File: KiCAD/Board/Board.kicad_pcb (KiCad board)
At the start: 2 copper layers, 141.2 x 154.3 mm, 104 parts, among them J1 MOTOR_5PIN_CONNECTOR, J3 BATTERY_2PIN_CONNECTOR, Q1 AO3400A, Q5 SFH309, Q7 AO3400A, Q8 SFH309, U1 4040, U10 ULN2003A, U11 CD4060BE, U2 4015, U3 LM393, U5 4040, U8 LM7805_TO220, U9 LM393, Y1 Crystal

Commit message: June 1st Updated
Greatly simplified design using ULN2003 completely and all of its pins. down to only 6 chips and 1 mosfet !!! . This will be  the last design modification. its perfect at this point
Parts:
- removed C13: C0.1uf, Capacitor_THT:C_Disc_D5.0mm_W2.5mm_P2.50mm
- removed C14: C10uf, Capacitor_THT:C_Radial_D6.3mm_H5.0mm_P2.50mm
- removed JP10, JP7, JP8, JP9: JMP, Library:Jumper
- removed Q8: SFH309, LED_THT:LED_D3.0mm_Clear
- removed R17, R19, R26, R27, R28, R30, R34, R35: R4.7K, Resistor_THT:R_Axial_DIN0207_L6.3mm_D2.5mm_P10.16mm_Horizontal
- removed U3: LM393, Package_DIP:DIP-8_W7.62mm_Socket
- added D11: D4148, Diode_THT:D_DO-35_SOD27_P12.70mm_Horizontal, F.Cu at (53.6, 133.8)
- added D12: D4148, Diode_THT:D_DO-35_SOD27_P12.70mm_Horizontal, F.Cu at (53.6, 137.3)
- added R2: R4.7K, Resistor_THT:R_Axial_DIN0207_L6.3mm_D2.5mm_P10.16mm_Horizontal, F.Cu at (53.6, 141.1)
- added R20: R47K, Resistor_THT:R_Axial_DIN0207_L6.3mm_D2.5mm_P10.16mm_Horizontal, F.Cu at (53.6, 145.2)
- added R22: R4.7K, Resistor_THT:R_Axial_DIN0207_L6.3mm_D2.5mm_P10.16mm_Horizontal, F.Cu at (53.6, 149.2)
- added R23: R4.7K, Resistor_THT:R_Axial_DIN0207_L6.3mm_D2.5mm_P10.16mm_Horizontal, F.Cu at (53.6, 153.3)
- Q1: value AO3400A -> SFH309; footprint Package_TO_SOT_SMD:SOT-23 -> LED_THT:LED_D3.0mm_Clear
- R13: value R47K -> R4.7K
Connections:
- D17 pad 1: Net-(D17-K) -> /F3
- D32 pad 1: Net-(D32-K) -> Net-(D15-K)
- D33 pad 1: Net-(D33-K) -> /F2
- Q1 pad 1: Net-(Q1-G) -> Net-(Q1-C)
- Q7 pad 3: Net-(Q5-C) -> Net-(Q1-C)
- R1 pad 1: Net-(D15-K) -> /LOAD
- R1 pad 2: Net-(Q1-G) -> +5V
- R13 pad 1: GND -> /R_RESET
- R13 pad 2: Net-(Q1-G) -> +5V
- R14 pad 1: Net-(Q1-D) -> /"R" CLOCK
- R14 pad 2: +5V -> Net-(D11-A)
- U10 pad 1: Net-(JP7-B) -> /F1
- U10 pad 10: unconnected-(U10-O7-Pad10) -> /F_RESET
- U10 pad 11: unconnected-(U10-O6-Pad11) -> /R_RESET
- U10 pad 12: unconnected-(U10-O5-Pad12) -> /LOAD
- U10 pad 5: unconnected-(U10-I5-Pad5) -> Net-(D15-K)
- U10 pad 6: unconnected-(U10-I6-Pad6) -> Net-(Q5-C)
- U10 pad 7: unconnected-(U10-I7-Pad7) -> Net-(Q1-C)
- U2 pad 15: Net-(Q1-D) -> /LOAD
- U2 pad 6: /F_RESET -> Net-(D11-K)
- U2 pad 7: Net-(Q1-D) -> /LOAD
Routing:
- net GND: track 265.9 -> 201.9 mm
- net +5V: track 168.2 -> 117.9 mm
- net Net-(JP1-B): track 38.5 -> 0.00 mm
- net Net-(Q5-C): track 26.4 -> 0.00 mm
- net Net-(U3B-+): track 7.75 -> 0.00 mm
- net Net-(Q8-C): track 4.17 -> 0.00 mm
- net Net-(D32-K): track 3.86 -> 0.00 mm
- net Net-(D15-K): track 11.7 -> 15.6 mm
- net /F_RESET: track 3.82 -> 0.00 mm
- net /R_RESET: track 3.56 -> 0.00 mm
- net /F1: track 17.0 -> 20.5 mm
- net Net-(JP7-B): track 3.55 -> 0.00 mm
- net Net-(D33-K): track 3.18 -> 0.00 mm
- net /F2: track 7.63 -> 10.8 mm
- net Net-(D17-K): track 3.05 -> 0.00 mm
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
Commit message: June 1st Project COMPLETED
Project Completed and Ready for Soldering
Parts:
- removed JP12: JMP, Library:Jumper
- added J2: MOTOR_5PIN_CONNECTOR_2, Connector_PinSocket_2.54mm:PinSocket_1x05_P2.54mm_Vertical, F.Cu at (92.2, 93.0)
- added JP10: JMP, Library:Jumper, F.Cu at (100.9, 96.7)
- added JP13: JMP, Library:Jumper, F.Cu at (59.2, 99.6)
- added JP14: JMP, Library:Jumper, F.Cu at (88.5, 96.5)
- added JP15: JMP, Library:Jumper, F.Cu at (27.8, 70.6)
- added JP16: JMP, Library:Jumper, F.Cu at (18.3, 84.3)
- added JP17: JMP, Library:Jumper, F.Cu at (16.6, 85.7)
- added JP19: JMP, Library:Jumper, F.Cu at (78.2, 23.8)
- added JP21: JMP, Library:Jumper, F.Cu at (93.1, 63.6)
- added JP7: JMP, Library:Jumper, F.Cu at (60.0, 124.0)
- added JP8: JMP, Library:Jumper, F.Cu at (18.1, 95.5)
- added JP9: JMP, Library:Jumper, F.Cu at (100.9, 94.1)
- added R17: R4.7K, Resistor_THT:R_Axial_DIN0207_L6.3mm_D2.5mm_P10.16mm_Horizontal, F.Cu at (129.2, 44.5)
- moved D1 154.0 mm to (122.4, 35.2), turned to -90 degrees
- moved D13 139.7 mm to (115.4, 35.2), turned to -90 degrees
- moved C4 106.9 mm to (119.2, 87.4), turned to 180 degrees
- moved C3 105.3 mm to (119.2, 92.8), turned to 180 degrees
- moved J3 105.2 mm to (116.7, 83.0), turned to 90 degrees
- moved U8 101.0 mm to (114.8, 99.6), turned to 180 degrees
- moved R2 98.3 mm to (108.1, 59.3), turned to -90 degrees
- moved JP6 91.6 mm to (138.3, 37.1), turned to 0 degrees
- moved C6 81.0 mm to (109.6, 88.6), turned to 0 degrees
- moved R22 75.4 mm to (103.8, 93.0), turned to 90 degrees
- moved C5 72.7 mm to (109.6, 82.7), turned to 0 degrees
- moved JP20 63.5 mm to (106.7, 30.3), turned to 0 degrees
- moved R20 56.7 mm to (39.1, 90.4), turned to 180 degrees
- moved R14 54.4 mm to (104.3, 59.3), turned to -90 degrees
- moved R23 50.9 mm to (74.9, 107.1)
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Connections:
- C1 pad 1: +5V -> /CLK_VCC
- C10 pad 1: +5V -> /CLK_VCC
- C2 pad 1: +5V -> /CLK_VCC
- C26 pad 1: Net-(JP6-A) -> +5V
- C27 pad 1: Net-(JP6-A) -> +5V
- C7 pad 1: Net-(JP6-A) -> +5V
- C8 pad 1: Net-(JP6-A) -> +5V
- C9 pad 1: +5V -> /CLK_VCC
- D1 pad 2: +5V -> /CLK_VCC
- D12 pad 2: /F_RESET -> Net-(D12-A)
- D13 pad 2: +5V -> /CLK_VCC
- D17 pad 1: /F3 -> Net-(D17-K)
- D2 pad 2: +5V -> Net-(D2-A)
- D32 pad 1: Net-(D15-K) -> Net-(D32-K)
- D33 pad 1: /F2 -> Net-(D33-K)
- J1 pad 1: Net-(J1-Pin_1) -> +5V
- JP20 pad 1: Net-(J1-Pin_1) -> +5V
- JP20 pad 2: +5V -> /CLK_VCC
- JP6 pad 1: Net-(JP6-A) -> +5V
- JP6 pad 2: +5V -> Net-(JP6-B)
- Q5 pad 1: Net-(Q5-C) -> Net-(JP7-B)
- R1 pad 1: /LOAD -> Net-(JP9-A)
- R13 pad 1: /R_RESET -> Net-(JP10-B)
- R14 pad 1: /"R" CLOCK -> Net-(U5-Q5)
- R14 pad 2: Net-(D11-A) -> /"R" CLOCK A
- R2 pad 1: Net-(Q5-C) -> Net-(U5-Q5)
- R2 pad 2: /"R" CLOCK -> /"R" CLOCK B
- R4 pad 1: Net-(JP6-A) -> +5V
- R8 pad 2: Net-(JP6-A) -> +5V
- R9 pad 2: +5V -> Net-(D2-A)
- U1 pad 16: Net-(JP6-A) -> +5V
- U10 pad 1: /F1 -> Net-(JP15-A)
- U10 pad 11: /R_RESET -> Net-(JP10-B)
- U10 pad 12: /LOAD -> Net-(JP9-A)
- U10 pad 5: Net-(D15-K) -> Net-(D32-K)
- U10 pad 6: Net-(Q5-C) -> Net-(JP7-B)
- U11 pad 16: Net-(JP6-A) -> +5V
- U2 pad 1: Net-(JP12-A) -> /MOTOR_CLOCK_B
- U5 pad 16: +5V -> /CLK_VCC
- U5 pad 2: /"R" CLOCK -> Net-(U5-Q5)
- U9 pad 4: GND -> Net-(JP21-A)
- U9 pad 8: +5V -> /CLK_VCC
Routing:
- net GND: track 201.9 -> 560.5 mm
- net Net-(JP6-A): track 73.8 -> 0.00 mm
- net +5V: track 117.9 -> 190.9 mm
- net /CLK_VCC: track 0.00 -> 47.3 mm
- net /F_RESET: track 0.00 -> 28.0 mm
- net Net-(Q1-D): track 27.6 -> 0.00 mm
- net Net-(JP1-B): track 0.00 -> 23.9 mm
- net /LOAD: track 0.00 -> 21.8 mm
- net Net-(JP10-B): track 0.00 -> 21.3 mm
- net Net-(Q1-C): track 0.00 -> 19.5 mm
- net /MOTOR_CLOCK_B: track 3.98 -> 22.1 mm
- net Net-(JP9-A): track 0.00 -> 15.4 mm
- net Net-(D11-K): track 0.00 -> 12.3 mm
- net Net-(D15-K): track 15.6 -> 3.38 mm
- net Net-(D31-A): track 12.7 -> 22.0 mm
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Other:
- board size 141.2 x 154.3 mm -> 122 x 87.5 mm
- board text added: "0BIT"
- board text added: "1BIT"
- board text added: "1MEG"
- board text added: "22pF x 2"
- board text added: "4040_11"
- board text added: "47K"
- board text added: "5V"
- board text added: "COMP7"
- board text added: "GND"
- board text added: "IR_DIODE"
- board text added: "IR_TRANSISTOR"
- board text added: "MCLKA"
- board text added: "RCLKA"
- board text added: "RCLKB"
- board text added: "ULN1"
- board text added: "ULN10"
- board text added: "ULN11"
- board text added: "ULN12"
- board text added: "ULN2"
- board text added: "ULN3"
- board text added: "ULN5"

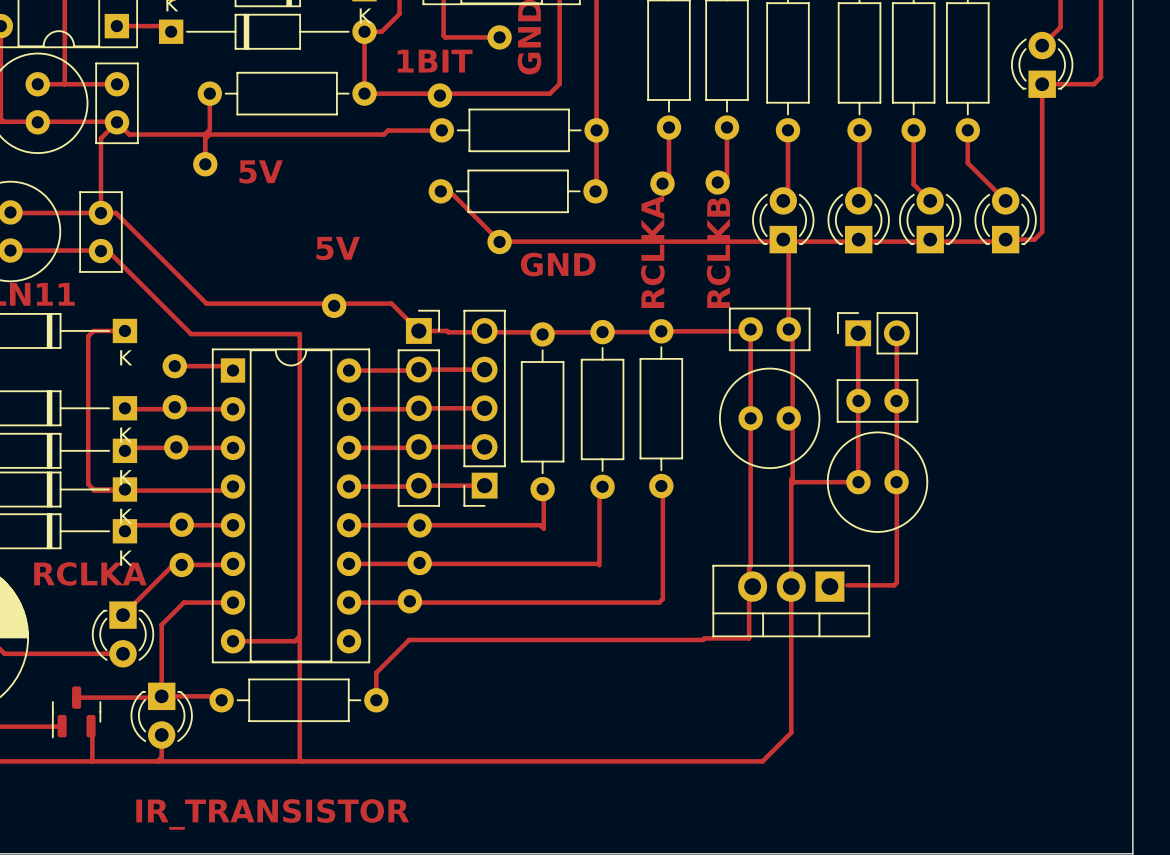
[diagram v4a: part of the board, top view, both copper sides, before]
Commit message: June 3rd 2025 Update
Added ULN2003 Pull down Resistors for Stepper Motor Control
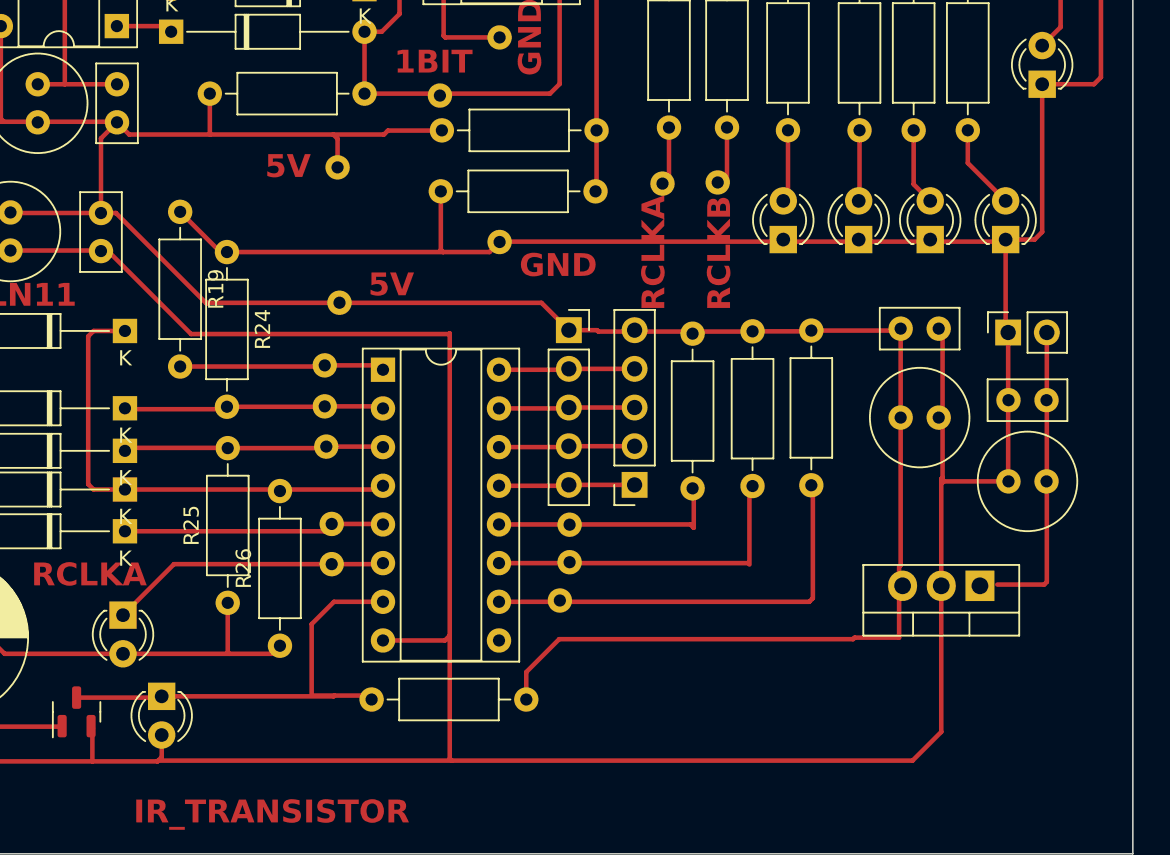
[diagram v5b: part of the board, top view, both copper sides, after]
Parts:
- added R19: R47K, Resistor_THT:R_Axial_DIN0207_L6.3mm_D2.5mm_P10.16mm_Horizontal, F.Cu at (72.2, 75.0)
- added R24: R47K, Resistor_THT:R_Axial_DIN0207_L6.3mm_D2.5mm_P10.16mm_Horizontal, F.Cu at (75.2, 77.6)
- added R25: R47K, Resistor_THT:R_Axial_DIN0207_L6.3mm_D2.5mm_P10.16mm_Horizontal, F.Cu at (75.3, 100.7)
- added R26: R47K, Resistor_THT:R_Axial_DIN0207_L6.3mm_D2.5mm_P10.16mm_Horizontal, F.Cu at (78.7, 103.5)
- moved C3 9.85 mm to (129.1, 92.7)
- moved C4 9.85 mm to (129.1, 87.4)
- moved C5 9.85 mm to (119.5, 82.7)
- moved C6 9.85 mm to (119.5, 88.5)
- moved J1 9.85 mm to (97.7, 82.8)
- moved J2 9.85 mm to (102.0, 92.9)
- moved J3 9.85 mm to (126.5, 82.9)
- moved R1 9.85 mm to (105.8, 93.2)
- moved R13 9.85 mm to (109.8, 93.0)
- moved R22 9.85 mm to (113.6, 93.0)
- moved R23 9.85 mm to (84.7, 107.0)
- moved U10 9.85 mm to (85.5, 85.4)
- moved U8 9.85 mm to (124.7, 99.6)
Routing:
- net GND: track 560.5 -> 616.5 mm
- net Net-(Q1-C): track 19.5 -> 30.9 mm
- net Net-(D32-K): track 7.26 -> 17.7 mm
- net /F2: track 7.62 -> 17.9 mm
- net /F3: track 7.37 -> 17.6 mm
- net +5V: track 190.9 -> 200.9 mm
- net Net-(JP7-B): track 8.62 -> 18.5 mm
- net Net-(JP15-A): track 3.93 -> 13.5 mm
- net /F4: track 24.0 -> 32.4 mm

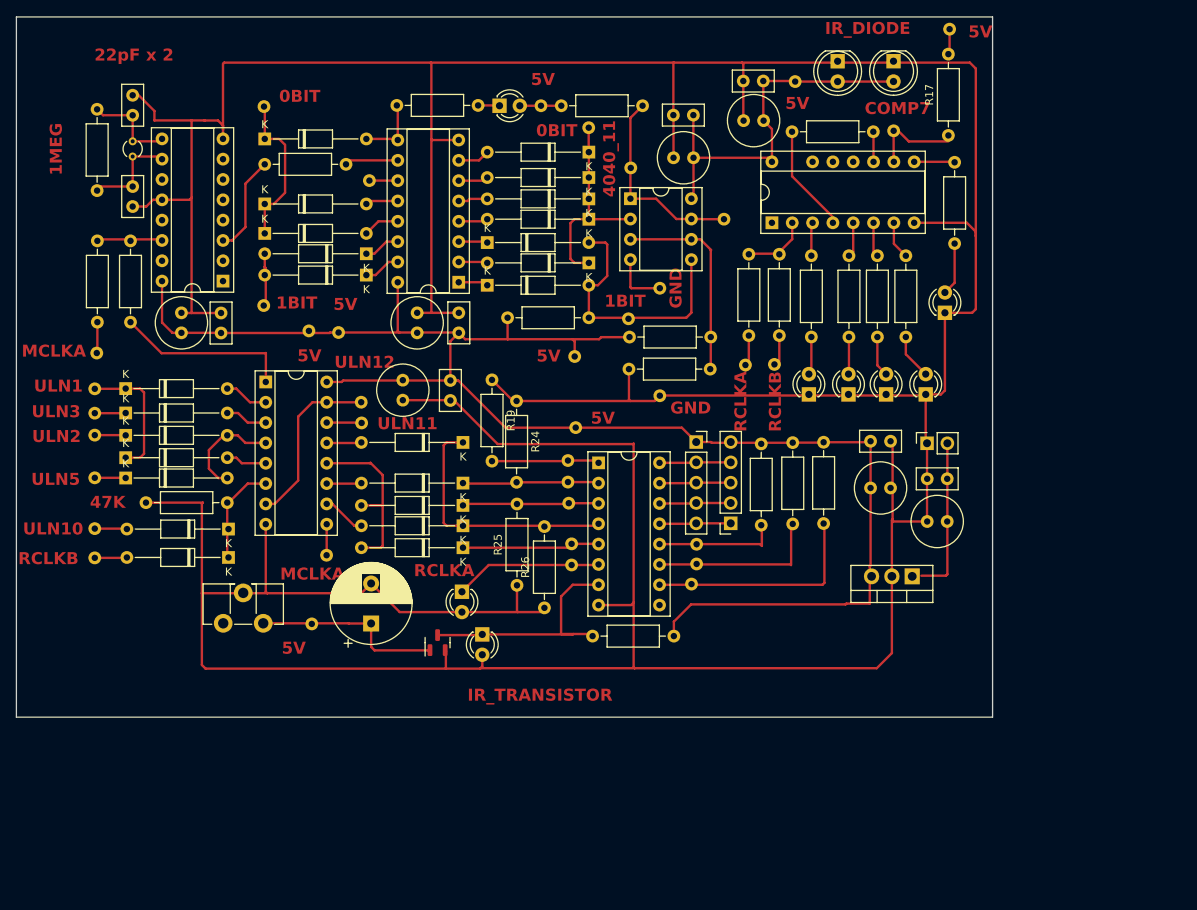
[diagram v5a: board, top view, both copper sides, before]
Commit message: 10th June 2025 Updated
Added Pull Downs 47K to ULN2003. Inverted Logic for Photo Transistors where cutting off IR rays off of photo transistors turns off forward and reverse motion since blocking IR rays is easier then reflecting it
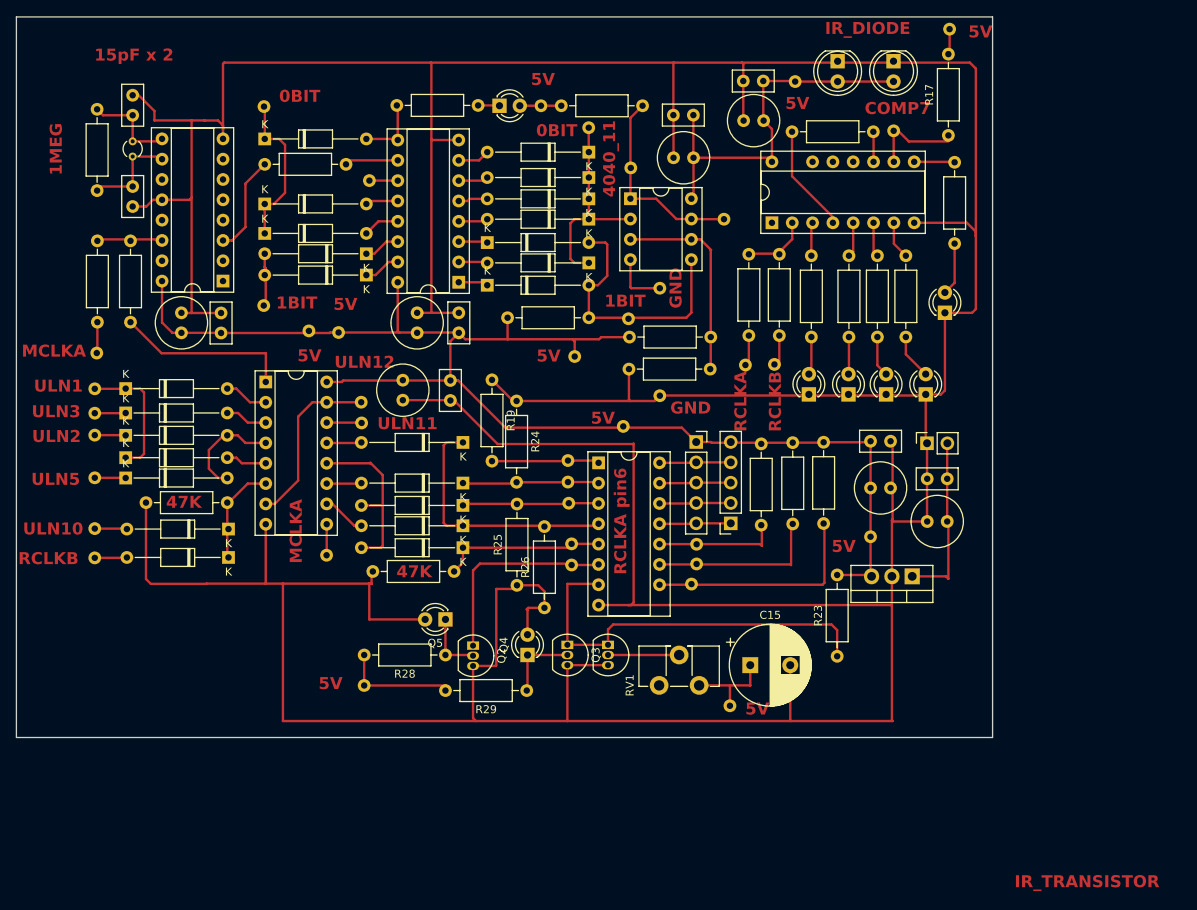
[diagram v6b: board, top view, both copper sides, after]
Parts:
- removed Q7: AO3400A, Package_TO_SOT_SMD:SOT-23
- added JP12: JMP, Library:Jumper, F.Cu at (84.1, 136.1)
- added Q2: BC547, Package_TO_SOT_THT:TO-92_Inline, F.Cu at (69.8, 108.2)
- added Q3: BC547, Package_TO_SOT_THT:TO-92_Inline, F.Cu at (81.6, 108.1)
- added Q4: SFH309, LED_THT:LED_D3.0mm_Clear, F.Cu at (76.6, 109.4)
- added R27: R47K, Resistor_THT:R_Axial_DIN0207_L6.3mm_D2.5mm_P10.16mm_Horizontal, F.Cu at (67.4, 99.0)
- added R28: R4.7K, Resistor_THT:R_Axial_DIN0207_L6.3mm_D2.5mm_P10.16mm_Horizontal, F.Cu at (66.3, 109.4)
- added R29: R4.7K, Resistor_THT:R_Axial_DIN0207_L6.3mm_D2.5mm_P10.16mm_Horizontal, F.Cu at (76.5, 113.8)
- Q1: value SFH309 -> BC547; footprint LED_THT:LED_D3.0mm_Clear -> Package_TO_SOT_THT:TO-92_Inline
- moved JP1 68.2 mm to (125.2, 126.8)
- moved RV1 55.0 mm to (93.1, 113.2)
- moved C15 47.7 mm to (104.4, 110.7), turned to 0 degrees
- moved R23 30.7 mm to (115.3, 109.6), turned to 90 degrees
- moved Q1 15.8 mm to (86.7, 108.1)
- moved Q5 4.03 mm to (66.3, 105.0), turned to 180 degrees
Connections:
- C15 pad 1: Net-(JP1-B) -> Net-(JP1-A)
- JP1 pad 1: +5V -> Net-(JP1-A)
- JP1 pad 2: Net-(JP1-B) -> +5V
- Q1 pad 2: GND -> Net-(Q1-B)
- Q5 pad 1: Net-(JP7-B) -> Net-(Q2-B)
- RV1 pad 2: GND -> Net-(Q1-B)
- RV1 pad 3: Net-(JP1-B) -> Net-(JP1-A)
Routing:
- net GND: track 616.5 -> 675.2 mm
- net +5V: track 200.9 -> 174.2 mm
- net Net-(JP1-B): track 23.9 -> 0.00 mm
- net Net-(Q1-C): track 30.9 -> 50.9 mm
- net Net-(JP12-A): track 0.00 -> 14.0 mm
- net Net-(JP1-A): track 0.00 -> 11.5 mm
- net Net-(Q3-B): track 0.00 -> 9.33 mm
- net Net-(Q1-B): track 0.00 -> 8.89 mm
- net Net-(Q2-B): track 0.00 -> 7.80 mm
- net Net-(JP7-B): track 18.5 -> 25.2 mm
- net Net-(D32-K): track 17.7 -> 20.5 mm
- net +8V: track 19.7 -> 21.4 mm
- net Net-(JP15-A): track 13.5 -> 12.5 mm
- net /F4: track 32.4 -> 31.5 mm
- net Net-(JP5-B): track 11.3 -> 10.7 mm
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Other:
- board size 122 x 87.5 mm -> 122 x 90.1 mm
- board text added: "15pF x 2"
- board text added: "RCLKA pin6"
- board text removed: "22pF x 2"
